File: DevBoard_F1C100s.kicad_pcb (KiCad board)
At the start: 2 copper layers, 192.8 x 140.2 mm, 51 parts, among them J101 USB_C_Receptacle_USB2.0_16P, J102 Conn_01x22, J103 Conn_01x11, J104 SD_Card, J105 UART0, J106 Conn_01x10, J108 Conn_01x05, J109 Conn_01x02, SW101 SW0, SW102 SW1, SW103 SW2, SW104 SW3, SW105 RESET, U101 AMS1117, U102 AMS1117-3.3, U103 TPS562201DDCT, U104 W25Q16JVSS, U105 F1C100s, Y101 24Mhz

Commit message: Layout: Almost complete
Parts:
- removed F101: 5V 2A, Jumper:SolderJumper-2_P1.3mm_Open_TrianglePad1.0x1.5mm
- removed J109: Conn_01x02, Connector_PinHeader_1.00mm:PinHeader_1x02_P1.00mm_Vertical_SMD_Pin1Left
- added TP1: TestPoint, TestPoint:TestPoint_Pad_D1.0mm, F.Cu at (140.3, 116.9)
- added TP2: TestPoint, TestPoint:TestPoint_Pad_D1.0mm, F.Cu at (151.5, 138.2)
- moved C104 161.3 mm to (189.7, 106.5), turned to -90 degrees
- moved C102 154.2 mm to (187.4, 101.2), turned to 0 degrees
- moved U102 154.1 mm to (184.1, 105.6), turned to 180 degrees
- moved C108 106.6 mm to (206.4, 108.2)
- moved C109 106.6 mm to (206.4, 110.7)
- moved C101 103.8 mm to (155.9, 99.3), turned to 0 degrees
- moved R102 96.0 mm to (135.8, 108.3), turned to 0 degrees
- moved R101 94.5 mm to (131.2, 108.3), turned to 0 degrees
- moved U101 87.7 mm to (132.0, 103.5), turned to 180 degrees
- moved C105 86.5 mm to (125.6, 104.3), turned to -90 degrees
- moved JP101 81.6 mm to (142.5, 101.7)
- moved U103 80.9 mm to (145.1, 105.5)
- moved L101 80.5 mm to (149.2, 106.3)
- moved C106 80.3 mm to (145.0, 108.4)
- moved C107 79.4 mm to (151.9, 106.3)
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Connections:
- C101 pad 1: /PWR_F -> /VUSB
- C102 pad 1: /PWR_F -> /VUSB
- C103 pad 1: /PWR_F -> /VUSB
- J101 pad A4: /VBUS -> /VUSB
- J101 pad A9: /VBUS -> /VUSB
- J101 pad B4: /VBUS -> /VUSB
- J101 pad B9: /VBUS -> /VUSB
- JP101 pad 2: /PWR_F -> /VUSB
- U101 pad 3: /PWR_F -> /VUSB
- U102 pad 3: /PWR_F -> /VUSB
- U103 pad 3: /PWR_F -> /VUSB
- U105 pad 67: /PWR_F -> /VUSB
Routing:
- net /3V3: track 0.00 -> 137.3 mm, vias 0 -> 6
- net /VUSB: track 0.00 -> 94.0 mm
- net /2V6: track 15.2 -> 80.2 mm, vias 0 -> 3
- net /SW3: track 17.6 -> 75.9 mm, vias 0 -> 2
- net /1V1: track 0.00 -> 55.3 mm, vias 0 -> 4
- net /SW2: track 19.1 -> 68.6 mm, vias 0 -> 2
- net /SW0: track 18.6 -> 56.2 mm, vias 0 -> 2
- net /SDC0_D2: track 0.00 -> 36.6 mm
- net /SW1: track 17.1 -> 53.4 mm, vias 0 -> 2
- net /SDC0_D0: track 0.00 -> 36.3 mm
- net /TVOUT: track 0.00 -> 36.3 mm
- net /SDC0_CMD: track 0.00 -> 36.1 mm
- net /SDC0_D1: track 0.00 -> 34.8 mm
- net /SDC0_D3: track 0.00 -> 34.6 mm
- net /SDC0_CLK: track 0.00 -> 34.4 mm
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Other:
- board outline removed

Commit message: Finish design
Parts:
- added R114: 10k, Resistor_SMD:R_0603_1608Metric_Pad0.98x0.95mm_HandSolder, F.Cu at (182.2, 118.5)
- added R115: 10k, Resistor_SMD:R_0603_1608Metric_Pad0.98x0.95mm_HandSolder, F.Cu at (182.2, 120.0)
- added R116: 10k, Resistor_SMD:R_0603_1608Metric_Pad0.98x0.95mm_HandSolder, F.Cu at (182.2, 121.5)
- added R117: 10k, Resistor_SMD:R_0603_1608Metric_Pad0.98x0.95mm_HandSolder, F.Cu at (182.2, 123.7)
- added R118: 10k, Resistor_SMD:R_0603_1608Metric_Pad0.98x0.95mm_HandSolder, F.Cu at (182.2, 128.9)
- added R119: 10k, Resistor_SMD:R_0603_1608Metric_Pad0.98x0.95mm_HandSolder, F.Cu at (184.0, 128.9)
- added TP3: TestPoint, TestPoint:TestPoint_Pad_D1.0mm, F.Cu at (185.1, 115.1)
- J104: value SD_Card -> Micro_SD_Card_Det1; footprint Connector_PinHeader_1.00mm:PinHeader_1x06_P1.00mm_Vertical_SMD_Pin1Left -> sd_card:sd_card_10p
- moved C110 37.6 mm to (125.6, 108.0), turned to -90 degrees
- moved C112 24.5 mm to (129.7, 98.8)
- moved C115 22.6 mm to (151.8, 109.2), turned to 180 degrees
- moved C113 19.1 mm to (152.1, 102.5), turned to 180 degrees
- moved C108 14.0 mm to (192.5, 106.5), turned to -90 degrees
- moved C109 11.8 mm to (195.4, 106.5), turned to -90 degrees
- moved J104 10.9 mm to (186.3, 129.4)
- moved SW105 0.85 mm to (159.3, 107.2)
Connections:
- J104 pad 1: /SDC0_D1 -> /SDC0_D2
- J104 pad 2: /SDC0_D0 -> /SDC0_D3
- J104 pad 3: /SDC0_CLK -> /SDC0_CMD
- J104 pad 4: /SDC0_CMD -> /3V3
- J104 pad 5: /SDC0_D3 -> /SDC0_CLK
- J104 pad 6: /SDC0_D2 -> GND
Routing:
- net /3V3: track 137.3 -> 200.8 mm, vias 6 -> 7
- net GND: track 3.47 -> 50.2 mm, vias 0 -> 36
- net /SDC0_D1: track 34.8 -> 59.0 mm
- net /SDC0_D0: track 36.3 -> 59.7 mm
- net /SDC0_CLK: track 34.4 -> 54.6 mm
- net /SDC0_CMD: track 36.1 -> 51.8 mm
- net /SDC0_D3: track 34.6 -> 45.7 mm
- net /2V6: track 80.2 -> 89.2 mm
- net /SDC0_D2: track 36.6 -> 43.3 mm
- net /1V1: track 55.3 -> 59.7 mm
- net /TV_VRN: track 30.2 -> 33.9 mm
- net Net-(J104-DET): track 0.00 -> 2.29 mm
- net /TVIN0: track 32.7 -> 34.0 mm
- net /LRADC0: track 17.6 -> 18.9 mm
- net /TVIN1: track 31.4 -> 32.7 mm
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- added copper zone on B.Cu, net GND
- added copper zone on F.Cu, net GND
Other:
- board outline added: 75 x 50 mm

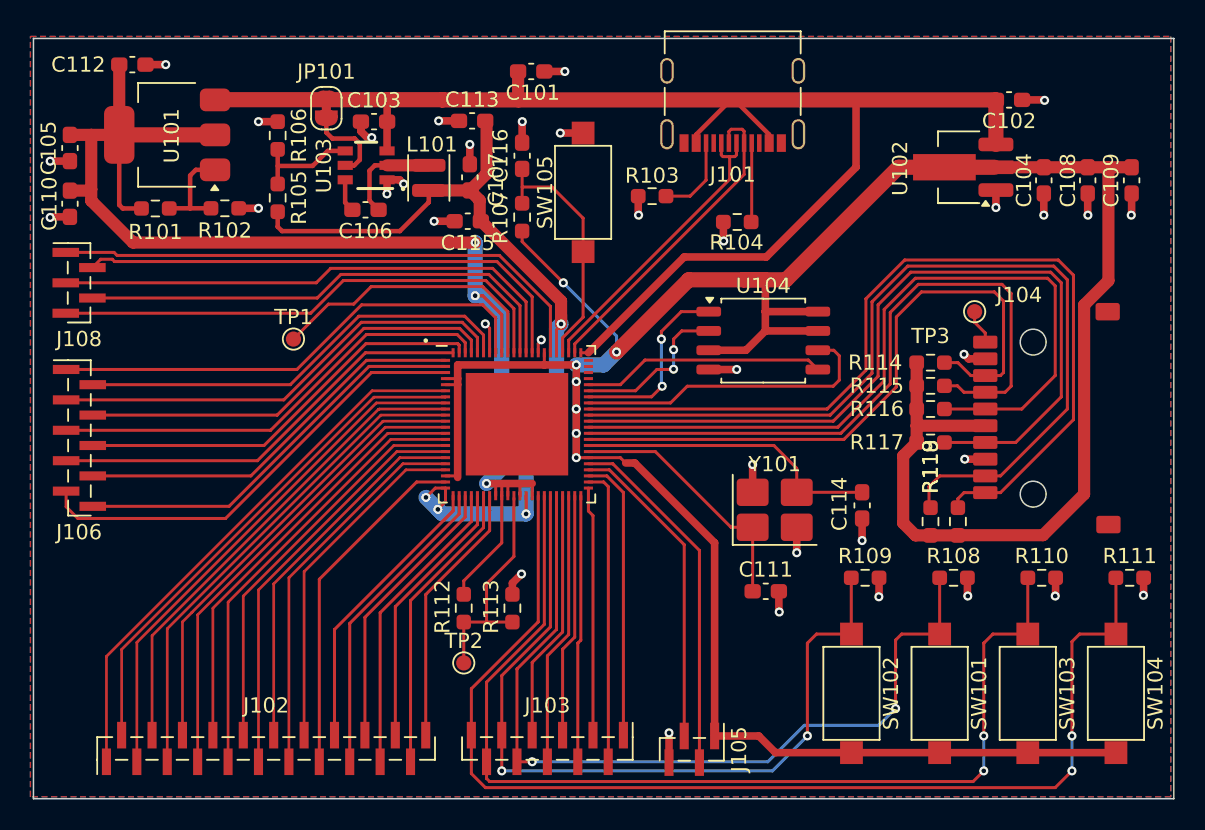
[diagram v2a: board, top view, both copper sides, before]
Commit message: Fix ground pour clearance
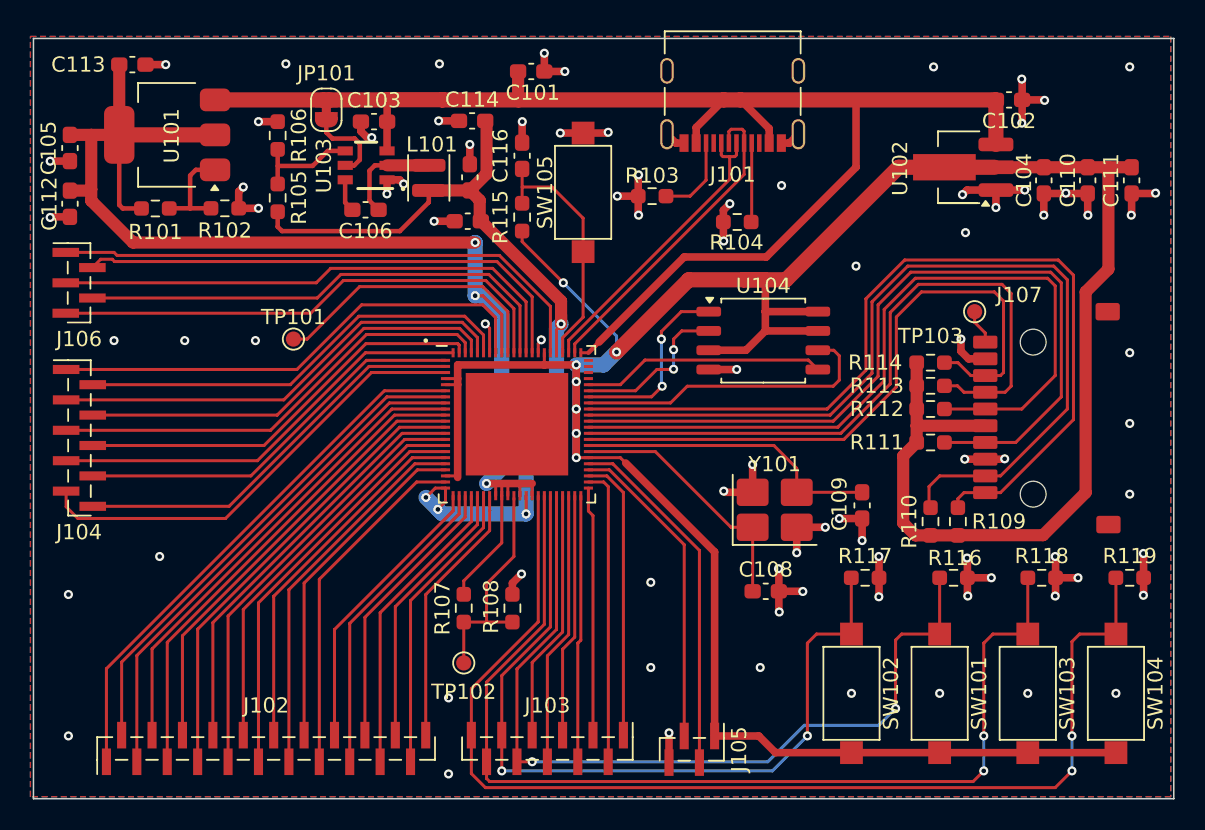
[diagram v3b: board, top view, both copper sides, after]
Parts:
- moved JP101 0.11 mm to (142.5, 101.8)
- renumbered C111 to C108, C114 to C109, C108 to C110, C109 to C111, C110 to C112, C112 to C113, C113 to C114, J106 to J104, J108 to J106, J104 to J107, R112 to R107, R113 to R108, R119 to R109, R118 to R110, R117 to R111, R116 to R112, R115 to R113, R107 to R115, R108 to R116, R109 to R117, R110 to R118, R111 to R119, TP1 to TP101, TP2 to TP102, TP3 to TP103
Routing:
- net GND: track 50.2 -> 92.7 mm, vias 36 -> 85
- net /VUSB: track 94.9 -> 94.3 mm
- net /PD7: track 28.4 -> 27.9 mm
- net /PD6: track 31.1 -> 30.5 mm
- net /PD5: track 30.2 -> 29.7 mm
- net /PD8: track 29.2 -> 28.7 mm
- net /PD4: track 32.9 -> 32.3 mm
- net /PD9: track 26.5 -> 26.0 mm
- net /PD3: track 32.0 -> 31.5 mm
- net /PD2: track 34.7 -> 34.2 mm
